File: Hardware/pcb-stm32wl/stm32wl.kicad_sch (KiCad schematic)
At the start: 69 parts, among them J7 U.FL/iPEX, U5 STM32WL55CCU6, U6 TS3A5223RSWR, U7 BGS13S4N9, X1 32MHz, Y1 32.768KHz

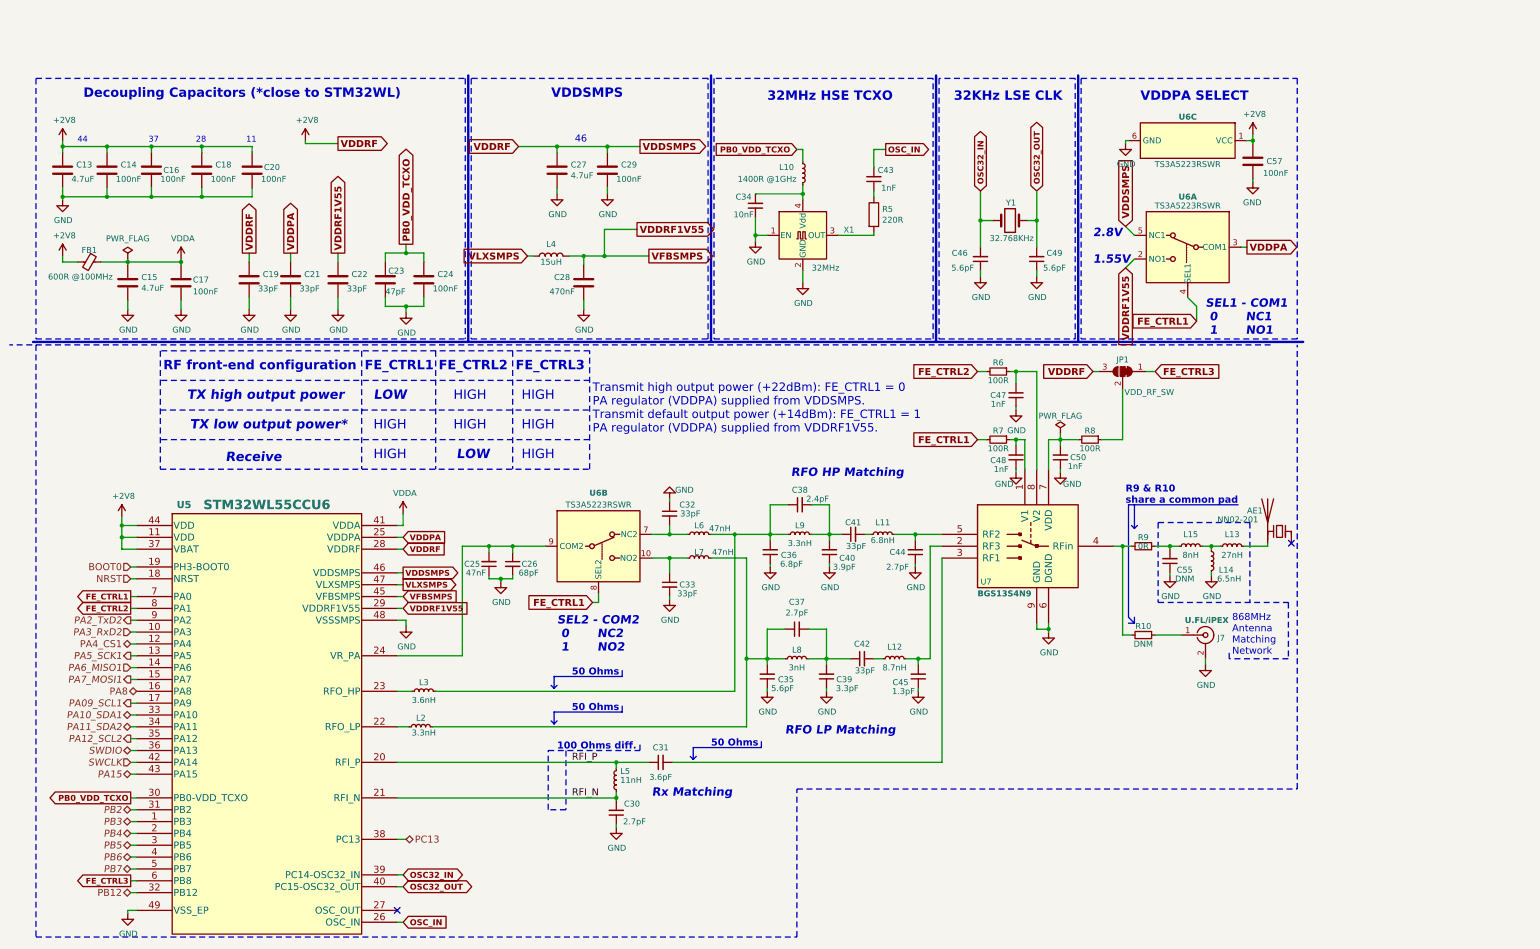
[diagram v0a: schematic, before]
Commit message: deleted some components today, finished selecting BUCK converter components for 5V
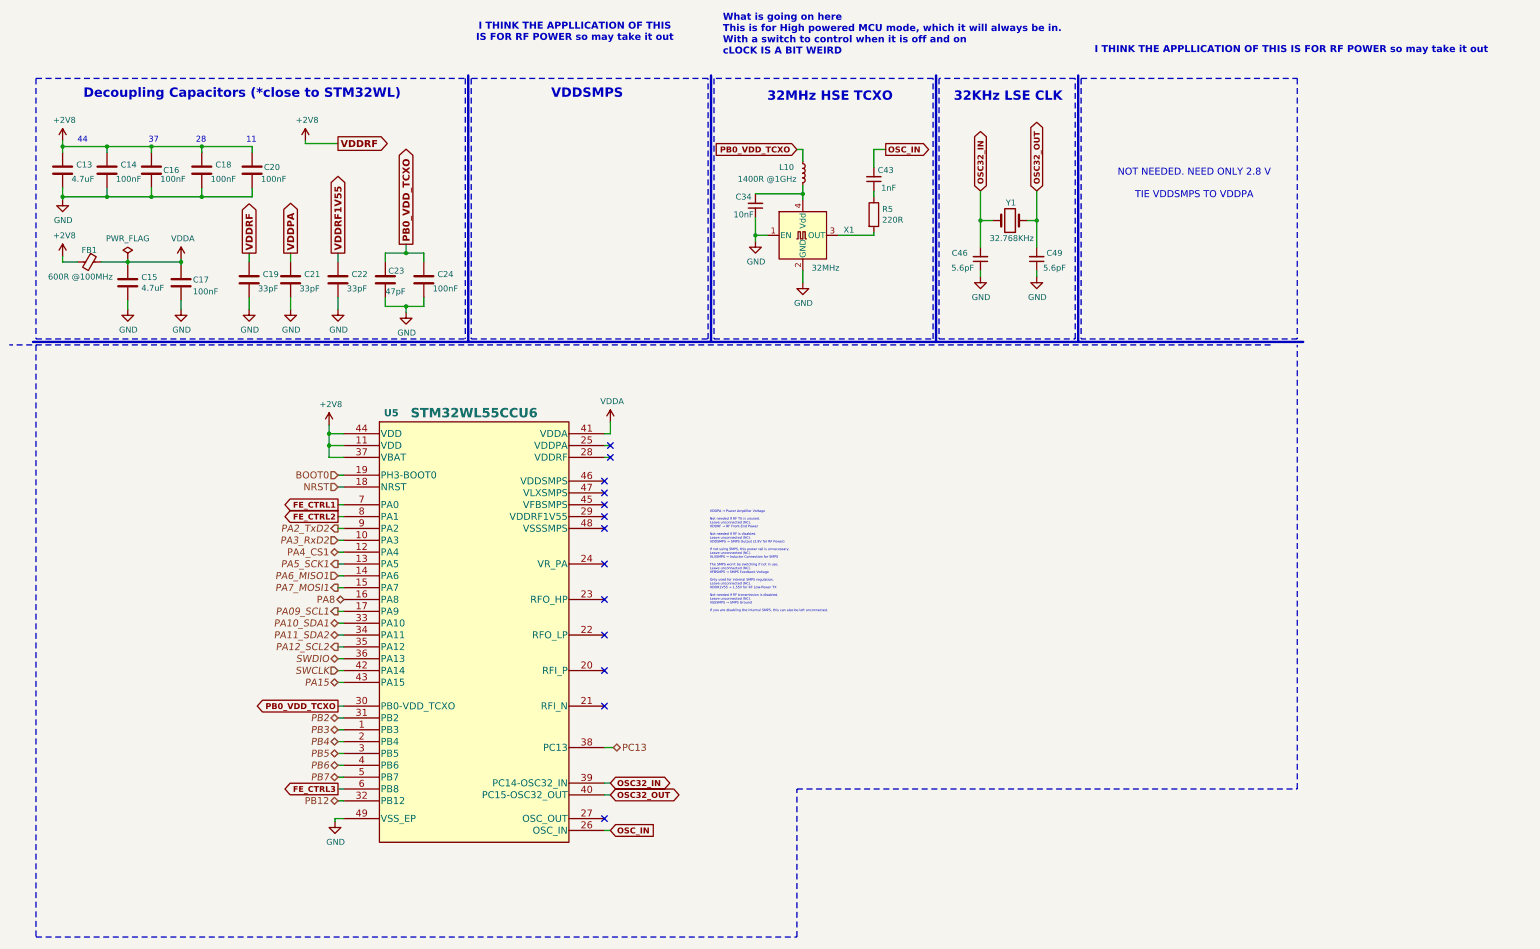
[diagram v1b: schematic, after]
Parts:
- removed AE1: NN02-201, node-lib-v1:Antenna_Fractus_NN02-201, symbol Device:Antenna_Chip
- removed C25: 47nF, Capacitor_SMD:C_0402_1005Metric, symbol Device:C_Small
- removed C26: 68pF, Capacitor_SMD:C_0402_1005Metric, symbol Device:C_Small
- removed C27: 4.7uF, Capacitor_SMD:C_0603_1608Metric, symbol Device:C
- removed C28: 470nF, Capacitor_SMD:C_0603_1608Metric, symbol Device:C
- removed C29, C57: 100nF, Capacitor_SMD:C_0402_1005Metric, symbol Device:C
- removed C30, C37, C44: 2.7pF, Capacitor_SMD:C_0402_1005Metric, symbol Device:C_Small
- removed C31: 3.6pF, Capacitor_SMD:C_0402_1005Metric, symbol Device:C_Small
- removed C32, C33, C41, C42: 33pF, Capacitor_SMD:C_0402_1005Metric, symbol Device:C_Small
- removed C35: 5.6pF, Capacitor_SMD:C_0402_1005Metric, symbol Device:C_Small
- removed C36: 6.8pF, Capacitor_SMD:C_0402_1005Metric, symbol Device:C_Small
- removed C38: 2.4pF, Capacitor_SMD:C_0402_1005Metric, symbol Device:C_Small
- removed C39: 3.3pF, Capacitor_SMD:C_0402_1005Metric, symbol Device:C_Small
- removed C40: 3.9pF, Capacitor_SMD:C_0402_1005Metric, symbol Device:C_Small
- removed C45: 1.3pF, Capacitor_SMD:C_0402_1005Metric, symbol Device:C_Small
- removed C47, C48, C50: 1nF, Capacitor_SMD:C_0402_1005Metric, symbol Device:C_Small
- removed C55: DNM, Capacitor_SMD:C_0402_1005Metric, symbol Device:C_Small
- removed J7: U.FL/iPEX, Connector_Coaxial:U.FL_Hirose_U.FL-R-SMT-1_Vertical, symbol Connector:Conn_Coaxial
- removed JP1: VDD_RF_SW, Jumper:SolderJumper-3_P1.3mm_Bridged12_RoundedPad1.0x1.5mm_NumberLabels, symbol Jumper:SolderJumper_3_Bridged12
- removed L11: 6.8nH, Inductor_SMD:L_0402_1005Metric, symbol Device:L_Small
- removed L12: 8.7nH, Inductor_SMD:L_0402_1005Metric, symbol Device:L_Small
- removed L13: 27nH, Inductor_SMD:L_0402_1005Metric, symbol Device:L_Small
- removed L14: 6.5nH, Inductor_SMD:L_0402_1005Metric, symbol Device:L_Small
- removed L15: 8nH, Inductor_SMD:L_0402_1005Metric, symbol Device:L_Small
- removed L2, L9: 3.3nH, Inductor_SMD:L_0402_1005Metric, symbol Device:L_Small
- removed L3: 3.6nH, Inductor_SMD:L_0402_1005Metric, symbol Device:L_Small
- removed L4: 15uH, node-lib-v1:L_0805_2012Metric_custom, symbol Device:L
- removed L5: 11nH, Inductor_SMD:L_0402_1005Metric, symbol Device:L_Small
- removed L6, L7: 47nH, Inductor_SMD:L_0402_1005Metric, symbol Device:L_Small
- removed L8: 3nH, Inductor_SMD:L_0402_1005Metric, symbol Device:L_Small
- removed R10: DNM, Resistor_SMD:R_0402_1005Metric, symbol Device:R_Small
- removed R6, R7, R8: 100R, Resistor_SMD:R_0402_1005Metric, symbol Device:R_Small
- removed R9: 0R, Resistor_SMD:R_0402_1005Metric, symbol Device:R_Small
- removed U6: TS3A5223RSWR, Package_DFN_QFN:UQFN-10_1.4x1.8mm_P0.4mm, symbol node-lib-v1:TS3A5223RSWR
- removed U7: BGS13S4N9, node-lib-v1:RFSW_BGS13S4N9E6327XTSA1, symbol node-lib-v1:BGS13S4N9
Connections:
- net +2V8: no longer U5.28 (VDDRF), U5.46 (VDDSMPS)
- net GND: no longer U5.48 (VSSSMPS)
- net VDDPA: no longer U5.25 (VDDPA)
- net VDDRF1V55: no longer U5.29 (VDDRF1V55), U5.45 (VFBSMPS)
- net RFI_N: no longer names the net of U5.21 (RFI_N)
- net RFI_P: no longer names the net of U5.20 (RFI_P)
- net VLXSMPS: no longer names the net of U5.47 (VLXSMPS)
- no-connect marks 2 -> 13
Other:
- note added: "I THINK THE APPLLICATION OF THIS IS FOR RF POWER so may take it out"
- note added: "NOT NEEDED. NEED ONLY 2.8 V TIE VDDSMPS TO VDDPA"
- note added: "VDDPA → Power Amplifier Voltage Not needed if RF TX is unused. Leave unconnected (NC). VDDRF → RF Front-End Power Not needed if RF is disabled. Leave unconnected (NC). VDDSMPS → SMPS Output (2.8V for RF Power) If not using SMPS, this power rail is unnecessary. Leave unconnected (NC). VLXSMPS → Inductor Connection for SMPS The SMPS won't be switching if not in use. Leave unconnected (NC). VFBSMPS 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"
- note added: "What is going on here This is for High powered MCU mode, which it will always be in. With a switch to control when it is off and on cLOCK IS A BIT WEIRD"
- note removed: "1.55V"
- note removed: "100 Ohms diff."
- note removed: "2.8V"
- note removed: "46"
- note removed: "50 Ohms"
- note removed: "868MHz Antenna Matching Network"
- note removed: "FE_CTRL1"
- note removed: "FE_CTRL2"
- note removed: "FE_CTRL3"
- note removed: "HIGH"
- note removed: "LOW"
- note removed: "R9 & R10 share a common pad"
- note removed: "RF front-end configuration"
- note removed: "RFO HP Matching"
- note removed: "RFO LP Matching"
- note removed: "Receive"
- note removed: "Rx Matching"
- note removed: "SEL1 - COM1 0 NC1 1 NO1"
- note removed: "SEL2 - COM2 0 NC2 1 NO2"
- note removed: "TX high output power"
- note removed: "TX low output power*"
- note removed: "Transmit high output power (+22dBm): FE_CTRL1 = 0 PA regulator (VDDPA) supplied from VDDSMPS. Transmit default output power (+14dBm): FE_CTRL1 = 1 PA regulator (VDDPA) supplied from VDDRF1V55."
- note removed: "VDDPA SELECT"
- moved on the sheet: U5
